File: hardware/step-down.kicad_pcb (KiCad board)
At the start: 2 copper layers, 40 x 40 mm, 37 parts, among them J1 STACK-UP-HIGH, J2 STACK-UP-HIGH, P1 Black, P2 Green, Q1 FDS8449, U1 ZXCT1086, U2 AOZ1212, U3 DRILL, U4 DRILL, U5 DRILL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

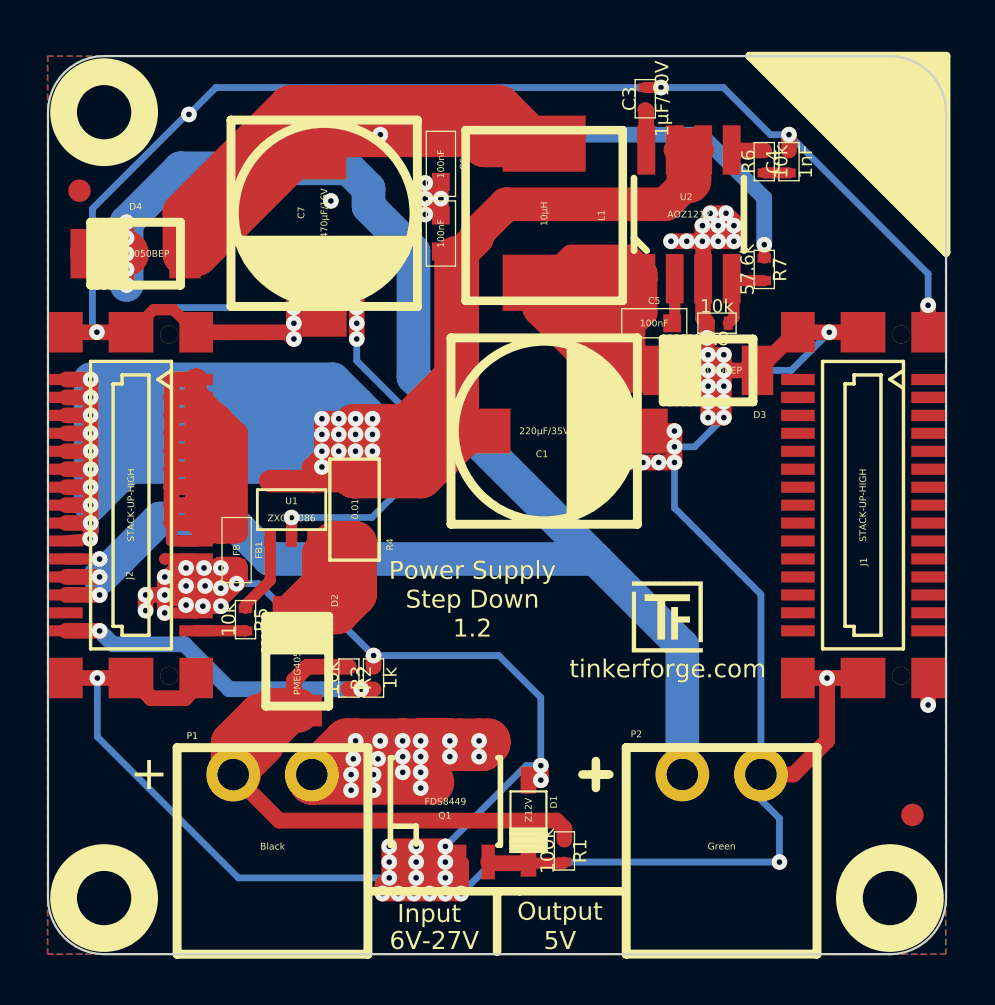
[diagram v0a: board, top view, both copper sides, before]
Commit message: Add 3d model (*.step and *.FCStd)
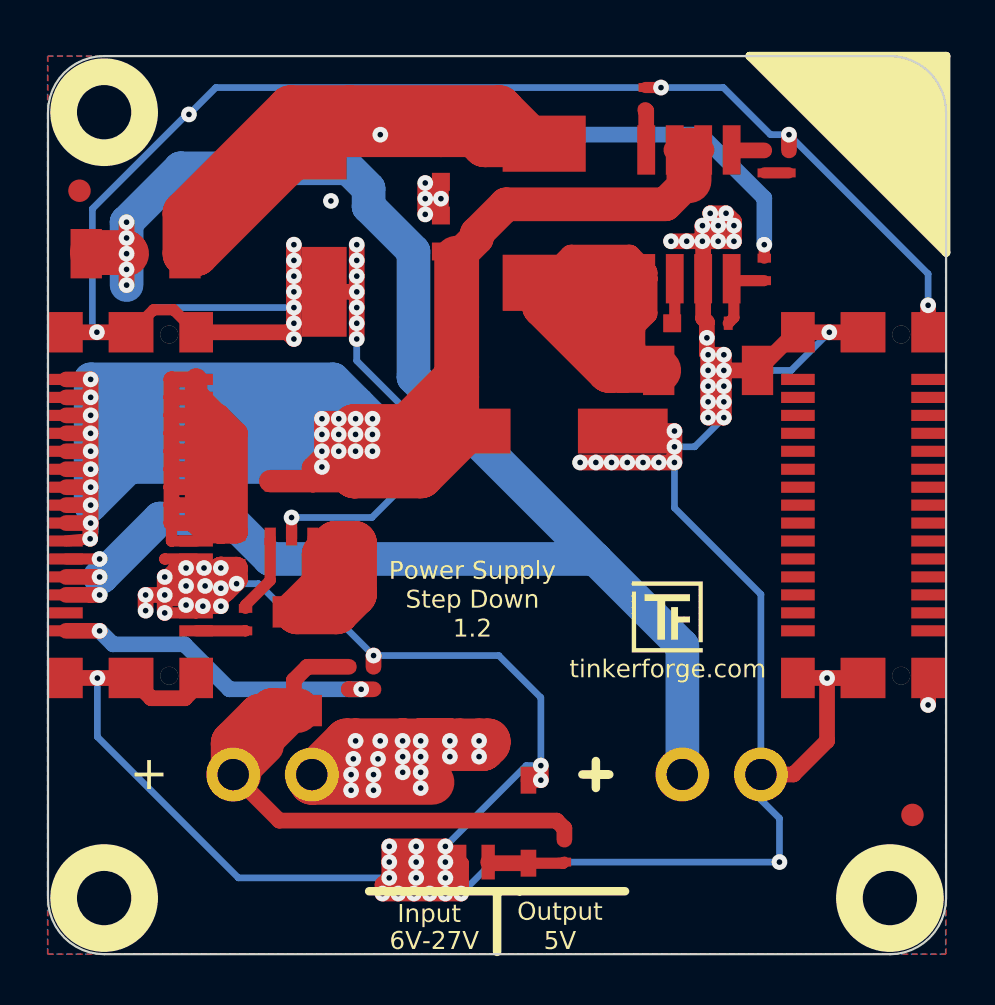
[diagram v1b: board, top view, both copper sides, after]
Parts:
- C2, C5, C6, FB1: footprint 0603 -> C0603
- C3, C4: footprint 0402 -> C0402
- Fiducial_Mark (x2): footprint Fiducial_Mark -> kicad-libraries:Fiducial_Mark
- R1, R2, R3, R5, R6, R7, R8: footprint 0402 -> R0402
- R4: footprint 1206 -> R1206
- VAL: footprint CE_5mm -> kicad-libraries:CE_5mm
- VAL: footprint WEEE_7mm -> kicad-libraries:WEEE_7mm
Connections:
- D1 pad 1: GND -> Net-(D1-Pad1)
- D1 pad 2: N-000001 -> GND
- J1 pad 1: (no net) -> Net-(J1-Pad1)
- J1 pad 10: (no net) -> Net-(J1-Pad10)
- J1 pad 11: (no net) -> Net-(J1-Pad11)
- J1 pad 12: (no net) -> Net-(J1-Pad12)
- J1 pad 13: (no net) -> Net-(J1-Pad13)
- J1 pad 14: (no net) -> Net-(J1-Pad14)
- J1 pad 15: (no net) -> Net-(J1-Pad15)
- J1 pad 16: (no net) -> Net-(J1-Pad16)
- J1 pad 17: (no net) -> Net-(J1-Pad17)
- J1 pad 18: (no net) -> Net-(J1-Pad18)
- J1 pad 19: (no net) -> Net-(J1-Pad19)
- J1 pad 2: (no net) -> Net-(J1-Pad2)
- J1 pad 20: (no net) -> Net-(J1-Pad20)
- J1 pad 21: (no net) -> Net-(J1-Pad21)
- J1 pad 22: (no net) -> Net-(J1-Pad22)
- J1 pad 23: (no net) -> Net-(J1-Pad23)
- J1 pad 24: (no net) -> Net-(J1-Pad24)
- J1 pad 25: (no net) -> Net-(J1-Pad25)
- J1 pad 26: (no net) -> Net-(J1-Pad26)
- J1 pad 27: (no net) -> Net-(J1-Pad27)
- J1 pad 28: (no net) -> Net-(J1-Pad28)
- J1 pad 29: (no net) -> Net-(J1-Pad29)
- J1 pad 3: (no net) -> Net-(J1-Pad3)
- J1 pad 30: (no net) -> Net-(J1-Pad30)
- J1 pad 4: (no net) -> Net-(J1-Pad4)
- J1 pad 5: (no net) -> Net-(J1-Pad5)
- J1 pad 6: (no net) -> Net-(J1-Pad6)
- J1 pad 7: (no net) -> Net-(J1-Pad7)
- J1 pad 8: (no net) -> Net-(J1-Pad8)
- J1 pad 9: (no net) -> Net-(J1-Pad9)
- J2 pad 28: (no net) -> Net-(J2-Pad28)
- Q1 pad G: N-000001 -> Net-(D1-Pad1)
- R1 pad 2: N-000001 -> Net-(D1-Pad1)
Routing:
- net Net-(D1-Pad1): track 0.00 -> 11.9 mm, vias 0 -> 2
- net GND: track 289.4 -> 281.0 mm, vias 92 -> 90
- net N-000001: track 3.44 -> 0.00 mm

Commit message: add new version of step down power supply
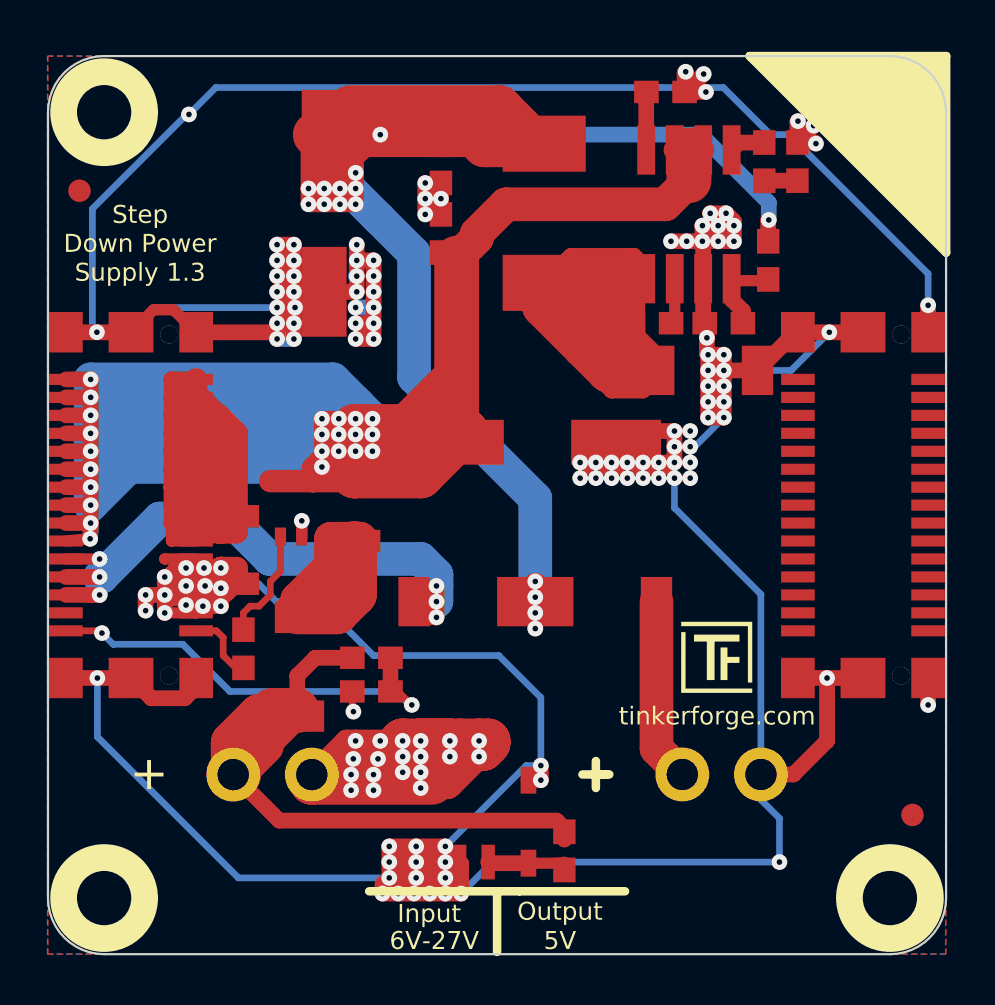
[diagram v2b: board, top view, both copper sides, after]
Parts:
- added D5: PMEG4050BEP, kicad-libraries:SOD-128, F.Cu at (155.5, 107.9)
- C1, C7: footprint ELKO_83 -> kicad-libraries:ELKO_83
- C2, C5, C6: footprint C0603 -> kicad-libraries:C0603E
- C3, C4: footprint C0402 -> kicad-libraries:C0603E
- D1: footprint SOD-123 -> kicad-libraries:SOD-123
- D2, D3, D4: footprint SOD-128 -> kicad-libraries:SOD-128
- FB1: footprint C0603 -> kicad-libraries:R1206
- J1, J2: footprint BTB08-ACS-TOP -> kicad-libraries:BTB08-ACS-TOP
- L1: footprint SRP7030 -> kicad-libraries:SRP7030
- P1, P2: footprint OQ_2P -> kicad-libraries:OQ_2P
- Q1: footprint SOIC-8-MOSFET -> kicad-libraries:SOIC-8-MOSFET
- R1, R2, R3, R5: footprint R0402 -> kicad-libraries:R0603E
- R4: footprint R1206 -> kicad-libraries:R1206
- R6, R7, R8: footprint R0402 -> kicad-libraries:C0603E
- U1: footprint SOT23-5 -> kicad-libraries:SOT23-5
- U2: footprint SO-8 -> kicad-libraries:SO-8
- U3, U4, U5, U6: footprint DRILL_NP -> kicad-libraries:DRILL_NP
- moved D4 21.3 mm to (149.1, 107.9)
- moved Ref** 2.84 mm to (158.8, 108.8)
- moved R2 1.35 mm to (145.0, 110.4), turned to 0 degrees
- moved R5 1.30 mm to (139.3, 110.0)
- moved C3 0.95 mm to (158.1, 85.2), turned to 0 degrees
- moved R3 0.60 mm to (145.0, 111.9), turned to 180 degrees
- moved C1 0.58 mm to (152.4, 100.8)
- moved U1 0.45 mm to (141.9, 103.8)
- moved R7 0.44 mm to (162.7, 92.7)
- moved C4 0.38 mm to (164.0, 88.3)
- moved R4 0.37 mm to (144.6, 103.7)
- moved R8 0.31 mm to (160.7, 95.5)
- moved D2 0.27 mm to (141.8, 110.8)
- moved FB1 0.20 mm to (139.2, 105.6), turned to 90 degrees
- moved C5 0.10 mm to (157.5, 95.5)
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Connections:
- D1 pad 1: Net-(D1-Pad1) -> GND
- D1 pad 2: GND -> Net-(D1-Pad2)
- FB1 pad 1: AGND -> GND
- FB1 pad 2: GND -> AGND
- J1 pad 1: Net-(J1-Pad1) -> (no net)
- J1 pad 10: Net-(J1-Pad10) -> (no net)
- J1 pad 11: Net-(J1-Pad11) -> (no net)
- J1 pad 12: Net-(J1-Pad12) -> (no net)
- J1 pad 13: Net-(J1-Pad13) -> (no net)
- J1 pad 14: Net-(J1-Pad14) -> (no net)
- J1 pad 15: Net-(J1-Pad15) -> (no net)
- J1 pad 16: Net-(J1-Pad16) -> (no net)
- J1 pad 17: Net-(J1-Pad17) -> (no net)
- J1 pad 18: Net-(J1-Pad18) -> (no net)
- J1 pad 19: Net-(J1-Pad19) -> (no net)
- J1 pad 2: Net-(J1-Pad2) -> (no net)
- J1 pad 20: Net-(J1-Pad20) -> (no net)
- J1 pad 21: Net-(J1-Pad21) -> (no net)
- J1 pad 22: Net-(J1-Pad22) -> (no net)
- J1 pad 23: Net-(J1-Pad23) -> (no net)
- J1 pad 24: Net-(J1-Pad24) -> (no net)
- J1 pad 25: Net-(J1-Pad25) -> (no net)
- J1 pad 26: Net-(J1-Pad26) -> (no net)
- J1 pad 27: Net-(J1-Pad27) -> (no net)
- J1 pad 28: Net-(J1-Pad28) -> (no net)
- J1 pad 29: Net-(J1-Pad29) -> (no net)
- J1 pad 3: Net-(J1-Pad3) -> (no net)
- J1 pad 30: Net-(J1-Pad30) -> (no net)
- J1 pad 4: Net-(J1-Pad4) -> (no net)
- J1 pad 5: Net-(J1-Pad5) -> (no net)
- J1 pad 6: Net-(J1-Pad6) -> (no net)
- J1 pad 7: Net-(J1-Pad7) -> (no net)
- J1 pad 8: Net-(J1-Pad8) -> (no net)
- J1 pad 9: Net-(J1-Pad9) -> (no net)
- J2 pad 28: Net-(J2-Pad28) -> (no net)
- P2 pad 1: +5V -> Net-(D5-Pad2)
- Q1 pad G: Net-(D1-Pad1) -> Net-(D1-Pad2)
- R1 pad 2: Net-(D1-Pad1) -> Net-(D1-Pad2)
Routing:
- net +5V: track 84.6 -> 29.4 mm, vias 8 -> 6
- net Net-(C6-Pad1): track 68.3 -> 102.4 mm, vias 2 -> 15
- net GND: track 281.0 -> 308.2 mm, vias 90 -> 119
- net Net-(D1-Pad1): track 11.9 -> 0.00 mm, vias 2 -> 0
- net AGND: track 42.4 -> 52.1 mm
- net Net-(C5-Pad1): track 28.3 -> 37.4 mm
- net Net-(D5-Pad2): track 0.00 -> 8.17 mm
- net VPP: track 158.0 -> 161.8 mm
- net Net-(D1-Pad2): track 0.00 -> 3.44 mm
- net Net-(P1-Pad2): track 52.6 -> 55.9 mm
- net VOLTAGE: track 16.4 -> 19.5 mm
- net Net-(R5-Pad1): track 3.58 -> 5.00 mm
- net CURRENT: track 2.20 -> 3.26 mm
- net Net-(D2-Pad2): track 11.7 -> 12.6 mm
- net Net-(C3-Pad1): track 1.80 -> 2.59 mm
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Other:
- board text added: "Step Down Power Supply 1.3"
- board text removed: "Power Supply Step Down 1.2"
